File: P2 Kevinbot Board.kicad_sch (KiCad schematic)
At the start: 13 parts, among them J1 Conn_01x03_Pin, J12 Conn_02x06_Odd_Even, J16 Conn_02x06_Odd_Even, J2 Conn_01x03_Pin, J6 Conn_02x06_Odd_Even, J8 Conn_02x06_Odd_Even, J9 Conn_01x02_Pin, SW1 SW_Push, U1 P2_EDGE_MODULE_SOCKET

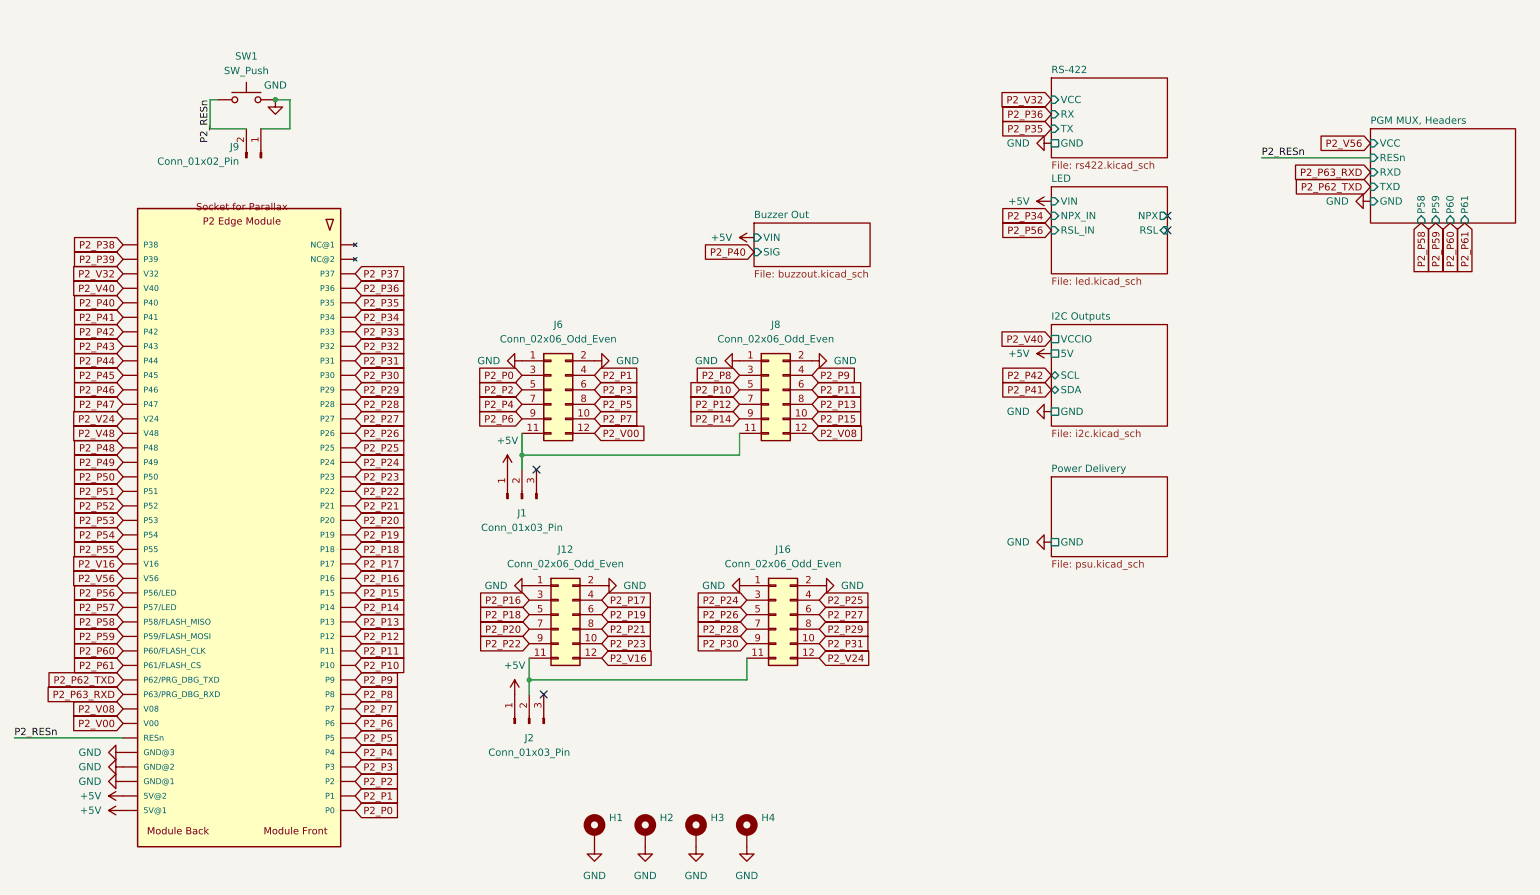
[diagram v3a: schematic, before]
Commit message: docs: add ibom, pcb, psu: fuse, pgmmux, pcb: 2.00mm headers -> 2.54
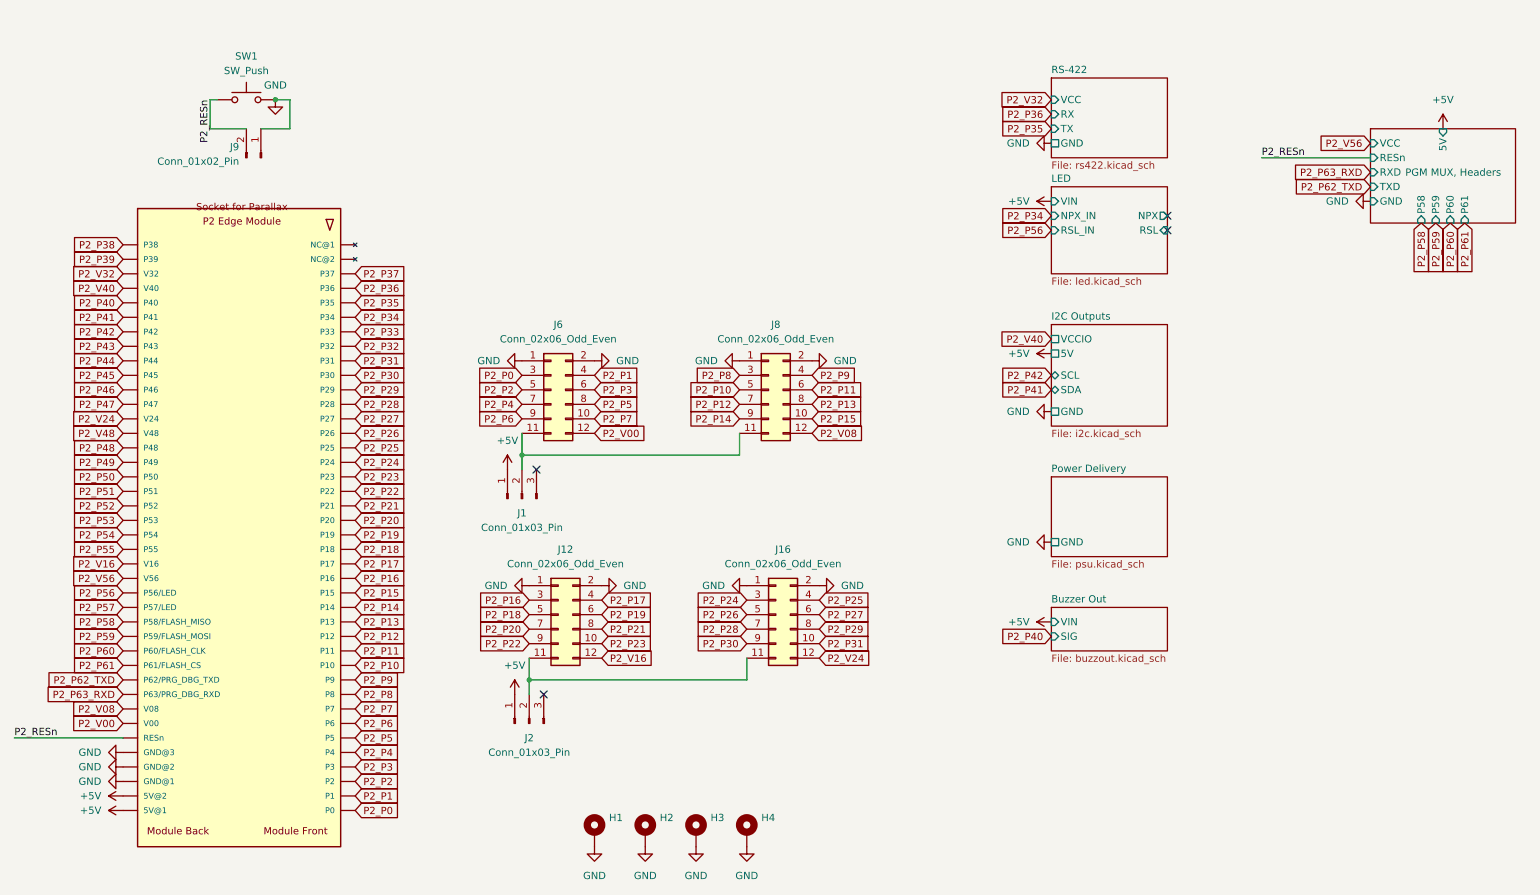
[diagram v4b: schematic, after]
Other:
- sheet PGM MUX, Headers ports: added 5V; removed none
- title: P2 Kevinbot Board -> Kevinbot Core
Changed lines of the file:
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@@
 	(paper "USLegal")
 	(title_block
-		(title "P2 Kevinbot Board")
-		(rev "A")
+		(title "Kevinbot Core")
+		(date "2025-04-12")
+		(rev "B-DEV")
 	)
 	(junction
@@
 	(global_label "P2_P40"
 		(shape input)
-		(at 156.21 55.88 180)
+		(at 208.28 123.19 180)
 		(fields_autoplaced yes)
 		(effects
@@
 		)
 		(property "Intersheetrefs" "${INTERSHEET_REFS}"
-			(at 146.6607 55.8006 0)
+			(at 198.7307 123.1106 0)
 			(effects
 				(font
@@
 	(symbol
 		(lib_id "power:+5V")
-		(at 156.21 53.34 90)
+		(at 208.28 120.65 90)
 		(unit 1)
 		(exclude_from_sim no)
@@
 		(fields_autoplaced yes)
 		(property "Reference" "#PWR028"
-			(at 160.02 53.34 0)
+			(at 212.09 120.65 0)
 			(effects
 				(font
@@
 		)
 		(property "Value" "+5V"
-			(at 152.4 53.3399 90)
+			(at 204.47 120.6499 90)
 			(effects
 				(font
@@
 		)
 		(property "Footprint" ""
-			(at 156.21 53.34 0)
+			(at 208.28 120.65 0)
 			(effects
 				(font
@@
 		)
 		(property "Datasheet" ""
-			(at 156.21 53.34 0)
+			(at 208.28 120.65 0)
 			(effects
 				(font
@@
 		)
 		(property "Description" "Power symbol creates a global label with name \"+5V\""
-			(at 156.21 53.34 0)
+			(at 208.28 120.65 0)
 			(effects
 				(font
@@
 	)
 	(symbol
+		(lib_id "power:+5V")
+		(at 276.86 34.29 0)
+		(unit 1)
+		(exclude_from_sim no)
+		(in_bom yes)
+		(on_board yes)
+		(dnp no)
+		(fields_autoplaced yes)
+		(property "Reference" "#PWR052"
+			(at 276.86 38.1 0)
+			(effects
+				(font
+					(size 1.27 1.27)
+				)
+				(hide yes)
+			)
+		)
+		(property "Value" "+5V"
+			(at 276.86 29.21 0)
+			(effects
+				(font
+					(size 1.27 1.27)
+				)
+			)
+		)
+		(property "Footprint" ""
+			(at 276.86 34.29 0)
+			(effects
+				(font
+					(size 1.27 1.27)
+				)
+				(hide yes)
+			)
+		)
+		(property "Datasheet" ""
+			(at 276.86 34.29 0)
+			(effects
+				(font
+					(size 1.27 1.27)
+				)
+				(hide yes)
+			)
+		)
+		(property "Description" "Power symbol creates a global label with name \"+5V\""
+			(at 276.86 34.29 0)
+			(effects
+				(font
+					(size 1.27 1.27)
+				)
+				(hide yes)
+			)
+		)
+		(pin "1"
+		)
+		(instances
+			(project "P2 Kevinbot Board"
+				(path "/362ca48c-0b77-4943-b8b3-fc15ab97f30d"
+					(reference "#PWR052")
+					(unit 1)
+				)
+			)
+		)
+	)
+	(symbol
 		(lib_id "power:GND")
 		(at 264.16 46.99 270)
@@
 		(on_board yes)
 		(dnp no)
-		(fields_autoplaced yes)
 		(stroke
 			(width 0.1524)
@@
 		)
 		(property "Sheetname" "PGM MUX, Headers"
-			(at 264.16 33.5784 0)
+			(at 270.256 42.672 0)
 			(effects
 				(font
@@
 			)
 		)
+		(pin "5V" input
+			(at 276.86 34.29 90)
+			(effects
+				(font
+					(size 1.27 1.27)
+				)
+				(justify right)
+			)
+		)
 		(instances
 			(project "P2 Kevinbot Board"
@@
 	)
 	(sheet
-		(at 156.21 50.8)
+		(at 208.28 118.11)
 		(size 20.32 7.62)
 		(exclude_from_sim no)
@@
 		)
 		(property "Sheetname" "Buzzer Out"
-			(at 156.21 50.0884 0)
+			(at 208.28 117.3984 0)
 			(effects
 				(font
@@
 		)
 		(property "Sheetfile" "buzzout.kicad_sch"
-			(at 156.21 59.0046 0)
+			(at 208.28 126.3146 0)
 			(effects
 				(font
@@
 		)
 		(pin "SIG" input
-			(at 156.21 55.88 180)
+			(at 208.28 123.19 180)
 			(effects
 				(font
@@
 		)
 		(pin "VIN" input
-			(at 156.21 53.34 180)
+			(at 208.28 120.65 180)
 			(effects
 				(font

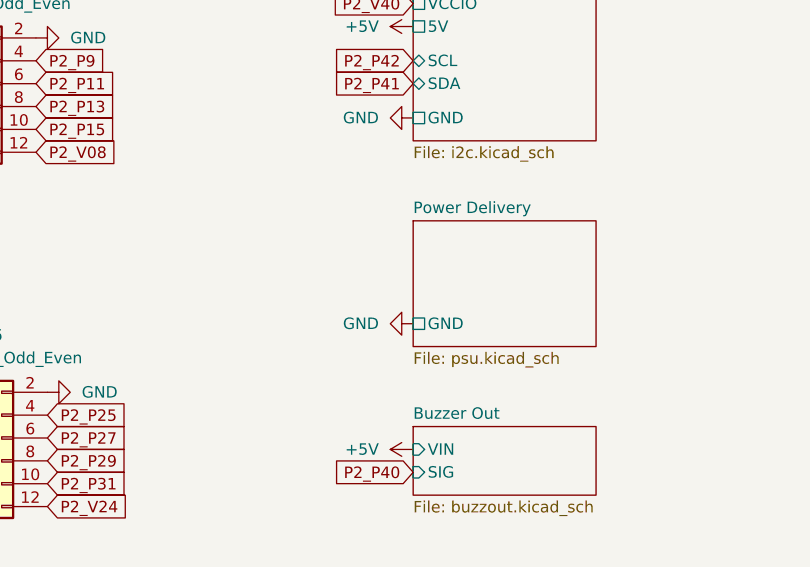
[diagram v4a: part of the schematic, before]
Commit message: sym: TMUX1511, psu: add failsafe development
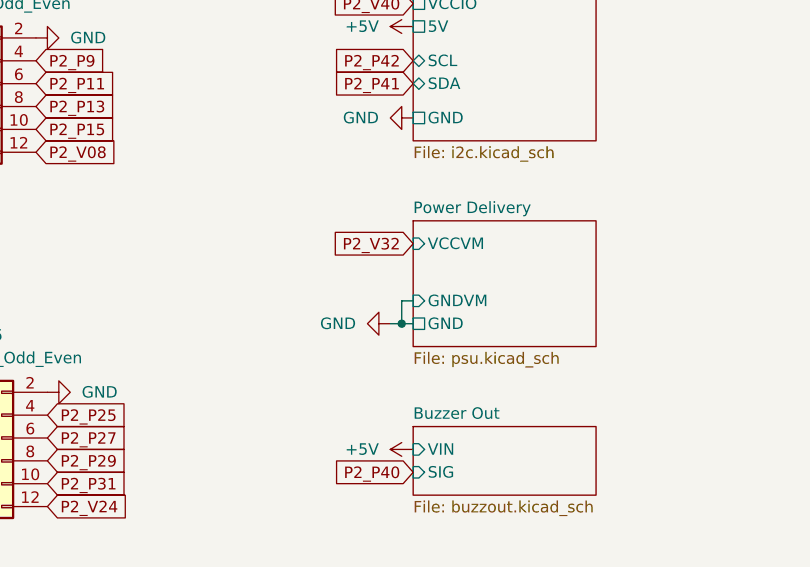
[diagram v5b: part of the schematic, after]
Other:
- sheet Power Delivery ports: added GNDVM, VCCVM; removed none
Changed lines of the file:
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@@
 		(color 0 0 0 0)
 	)
+	(junction
+		(at 207.01 106.68)
+		(diameter 0)
+		(color 0 0 0 0)
+	)
 	(no_connect
 		(at 228.6 49.53)
@@
 	(wire
 		(pts
+			(xy 207.01 106.68) (xy 208.28 106.68)
+		)
+		(stroke
+			(width 0)
+			(type default)
+		)
+	)
+	(wire
+		(pts
 			(xy 60.96 29.21) (xy 62.23 29.21)
 		)
@@
 	(wire
 		(pts
+			(xy 208.28 104.14) (xy 207.01 104.14)
+		)
+		(stroke
+			(width 0)
+			(type default)
+		)
+	)
+	(wire
+		(pts
+			(xy 207.01 104.14) (xy 207.01 106.68)
+		)
+		(stroke
+			(width 0)
+			(type default)
+		)
+	)
+	(wire
+		(pts
 			(xy 115.57 91.44) (xy 153.67 91.44)
 		)
@@
 		)
 	)
+	(wire
+		(pts
+			(xy 205.74 106.68) (xy 207.01 106.68)
+		)
+		(stroke
+			(width 0)
+			(type default)
+		)
+	)
 	(label "P2_RESn"
 		(at 245.11 39.37 0)
@@
 		)
 	)
+	(global_label "P2_V32"
+		(shape input)
+		(at 208.28 97.79 180)
+		(fields_autoplaced yes)
+		(effects
+			(font
+				(size 1.27 1.27)
+			)
+			(justify right)
+		)
+		(property "Intersheetrefs" "${INTERSHEET_REFS}"
+			(at 198.9121 97.7106 0)
+			(effects
+				(font
+					(size 1.27 1.27)
+				)
+				(justify right)
+				(hide yes)
+			)
+		)
+	)
 	(global_label "P2_P8"
 		(shape input)
@@
 	(symbol
 		(lib_id "power:GND")
-		(at 208.28 106.68 270)
+		(at 205.74 106.68 270)
 		(unit 1)
 		(exclude_from_sim no)
@@
 		(on_board yes)
 		(dnp no)
-		(fields_autoplaced yes)
 		(property "Reference" "#PWR050"
-			(at 201.93 106.68 0)
+			(at 199.39 106.68 0)
 			(effects
 				(font
@@
 		)
 		(property "Value" "GND"
-			(at 204.47 106.6799 90)
+			(at 201.93 106.6799 90)
 			(effects
 				(font
@@
 		)
 		(property "Footprint" ""
-			(at 208.28 106.68 0)
+			(at 205.74 106.68 0)
 			(effects
 				(font
@@
 		)
 		(property "Datasheet" ""
-			(at 208.28 106.68 0)
+			(at 205.74 106.68 0)
 			(effects
 				(font
@@
 		)
 		(property "Description" "Power symbol creates a global label with name \"GND\" , ground"
-			(at 208.28 106.68 0)
+			(at 205.74 106.68 0)
 			(effects
 				(font
@@
 			(effects
 				(font
+					(size 1.27 1.27)
+				)
+				(justify left)
+			)
+		)
+		(pin "GNDVM" input
+			(at 208.28 104.14 180)
+			(effects
+				(font
+					(size 1.27 1.27)
+				)
+				(justify left)
+			)
+		)
+		(pin "VCCVM" input
+			(at 208.28 97.79 180)
+			(effects
+				(font

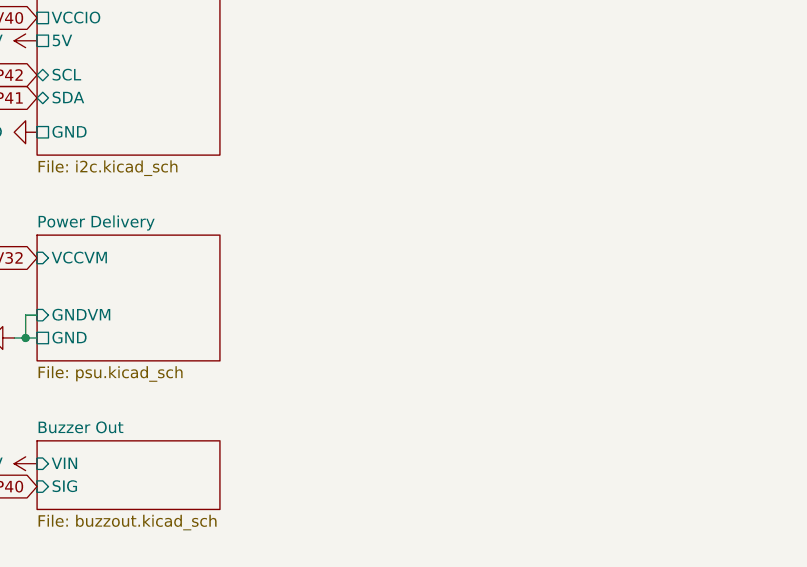
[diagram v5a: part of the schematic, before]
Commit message: psu, sch, pcb: voltmeters
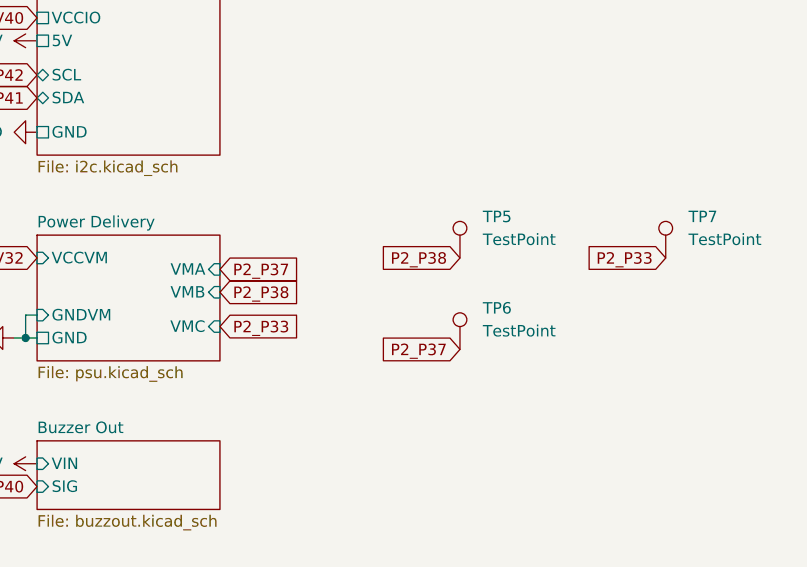
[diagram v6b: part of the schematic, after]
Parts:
- added TP5, TP6, TP7: TestPoint, TestPoint:TestPoint_Pad_D1.0mm, symbol Connector:TestPoint
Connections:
- net P2_P33: now also TP7.1
- net P2_P37: now also TP6.1
- net P2_P38: now also TP5.1
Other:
- sheet Power Delivery ports: added VMA, VMB, VMC; removed none

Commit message: sch, pcb: add part numbers
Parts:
- TP5, TP6, TP7: now left out of the parts list
- U1: MANUFACTURER Parallax : P2-EC -> (none); Part Number (none) -> 450-00308
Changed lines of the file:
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@@
 		(unit 1)
 		(exclude_from_sim no)
-		(in_bom yes)
+		(in_bom no)
 		(on_board yes)
 		(dnp no)
@@
 		(unit 1)
 		(exclude_from_sim no)
-		(in_bom yes)
+		(in_bom no)
 		(on_board yes)
 		(dnp no)
@@
 		(unit 1)
 		(exclude_from_sim no)
-		(in_bom yes)
+		(in_bom no)
 		(on_board yes)
 		(dnp no)
@@
 			)
 		)
-		(property "MANUFACTURER" "Parallax : P2-EC"
-			(at 49.53 168.91 0)
-			(effects
-				(font
-					(size 1.27 1.27)
-				)
-				(justify left bottom)
-				(hide yes)
-			)
+		(property "Part Number" "450-00308"
+			(at 66.04 104.14 0)
+			(effects
+				(font
+					(size 1.27 1.27)
+				)
+				(hide yes)
+			)

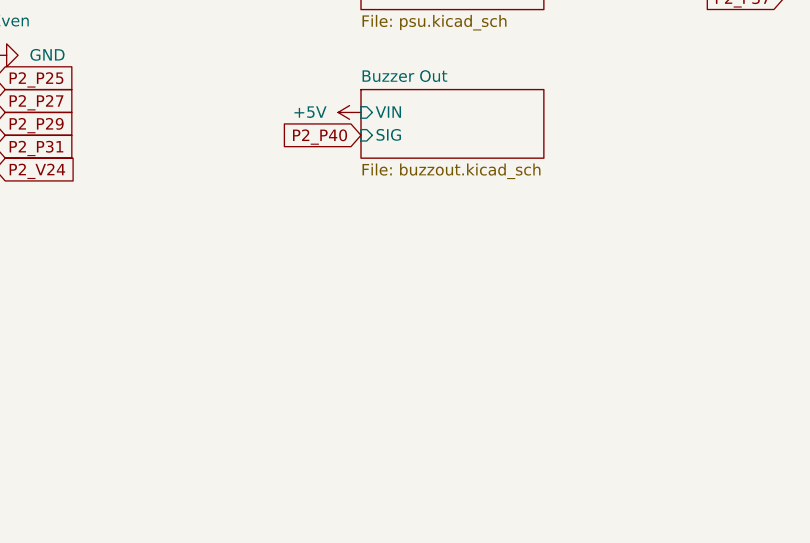
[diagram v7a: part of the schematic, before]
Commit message: owx, pcb: add one wire
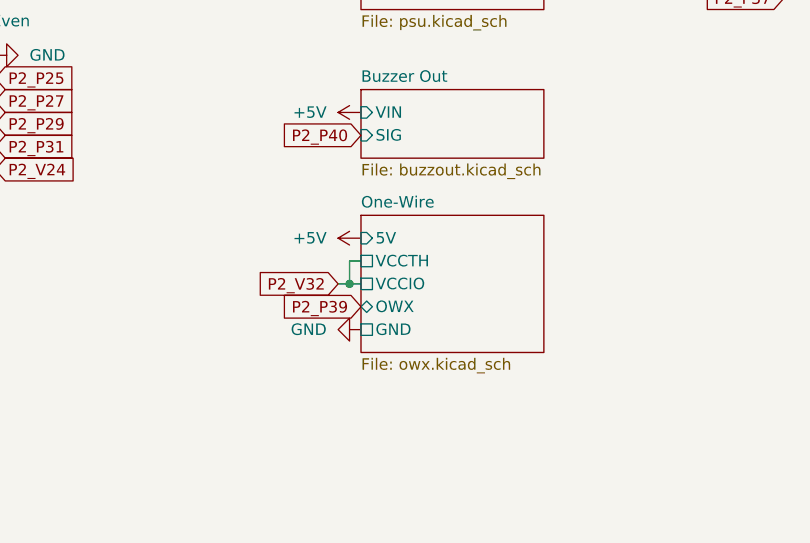
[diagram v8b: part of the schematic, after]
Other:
- added sheet One-Wire (owx.kicad_sch)
